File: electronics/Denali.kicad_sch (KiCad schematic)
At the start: 1 part, among them U1 kb2040

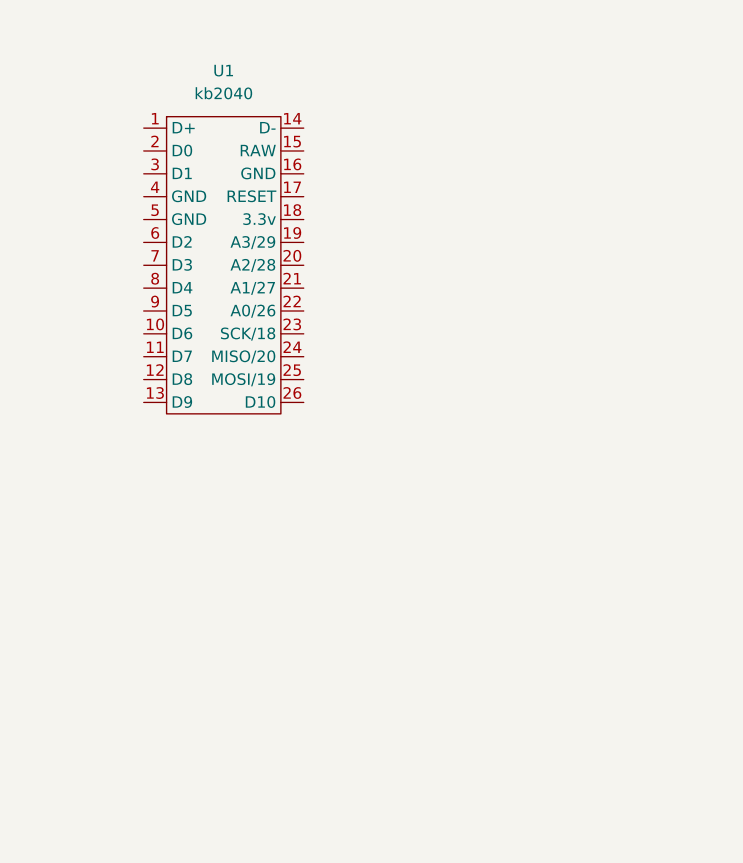
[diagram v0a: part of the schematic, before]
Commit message: add i2c headers to schematic
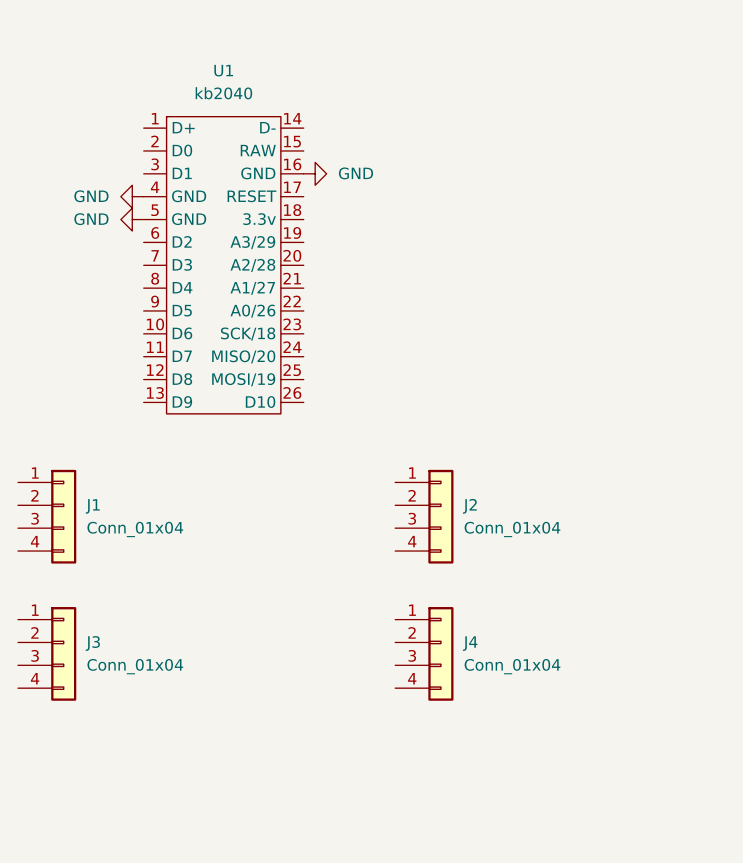
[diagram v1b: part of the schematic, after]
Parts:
- added J1, J2, J3, J4: Conn_01x04, symbol Connector_Generic:Conn_01x04
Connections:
- net GND: now reaches U1.16 (GND)
- net GND: now also U1.4 (GND), U1.5 (GND)
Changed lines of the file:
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@@
     (company "OSHMount Tech")
+  )
+  (symbol (lib_id "Connector_Generic:Conn_01x04") (at 36.83 92.71 0) (unit 1)
+    (in_bom yes) (on_board yes) (fields_autoplaced)
+    (property "Reference" "J3" (id 0) (at 39.37 92.7099 0)
+      (effects (font (size 1.27 1.27)) (justify left))
+    )
+    (property "Value" "Conn_01x04" (id 1) (at 39.37 95.2499 0)
+      (effects (font (size 1.27 1.27)) (justify left))
+    )
+    (property "Footprint" "" (id 2) (at 36.83 92.71 0)
+      (effects (font (size 1.27 1.27)) hide)
+    )
+    (property "Datasheet" "~" (id 3) (at 36.83 92.71 0)
+      (effects (font (size 1.27 1.27)) hide)
+    )
+    (pin "1")
+    (pin "2")
+    (pin "3")
+    (pin "4")
+  )
+  (symbol (lib_id "power:GND") (at 63.5 40.64 90) (unit 1)
+    (in_bom yes) (on_board yes) (fields_autoplaced)
+    (property "Reference" "#PWR01" (id 0) (at 69.85 40.64 0)
+      (effects (font (size 1.27 1.27)) hide)
+    )
+    (property "Value" "GND" (id 1) (at 67.31 40.6399 90)
+      (effects (font (size 1.27 1.27)) (justify right))
+    )
+    (property "Footprint" "" (id 2) (at 63.5 40.64 0)
+      (effects (font (size 1.27 1.27)) hide)
+    )
+    (property "Datasheet" "" (id 3) (at 63.5 40.64 0)
+      (effects (font (size 1.27 1.27)) hide)
+    )
+    (pin "1")
+  )
+  (symbol (lib_id "power:GND") (at 45.72 43.18 270) (unit 1)
+    (in_bom yes) (on_board yes) (fields_autoplaced)
+    (property "Reference" "#PWR02" (id 0) (at 39.37 43.18 0)
+      (effects (font (size 1.27 1.27)) hide)
+    )
+    (property "Value" "GND" (id 1) (at 41.91 43.1799 90)
+      (effects (font (size 1.27 1.27)) (justify right))
+    )
+    (property "Footprint" "" (id 2) (at 45.72 43.18 0)
+      (effects (font (size 1.27 1.27)) hide)
+    )
+    (property "Datasheet" "" (id 3) (at 45.72 43.18 0)
+      (effects (font (size 1.27 1.27)) hide)
+    )
+    (pin "1")
+  )
+  (symbol (lib_id "Connector_Generic:Conn_01x04") (at 78.74 77.47 0) (unit 1)
+    (in_bom yes) (on_board yes) (fields_autoplaced)
+    (property "Reference" "J2" (id 0) (at 81.28 77.4699 0)
+      (effects (font (size 1.27 1.27)) (justify left))
+    )
+    (property "Value" "Conn_01x04" (id 1) (at 81.28 80.0099 0)
+      (effects (font (size 1.27 1.27)) (justify left))
+    )
+    (property "Footprint" "" (id 2) (at 78.74 77.47 0)
+      (effects (font (size 1.27 1.27)) hide)
+    )
+    (property "Datasheet" "~" (id 3) (at 78.74 77.47 0)
+      (effects (font (size 1.27 1.27)) hide)
+    )
+    (pin "1")
+    (pin "2")
+    (pin "3")
+    (pin "4")
+  )
+  (symbol (lib_id "power:GND") (at 45.72 45.72 270) (unit 1)
+    (in_bom yes) (on_board yes) (fields_autoplaced)
+    (property "Reference" "#PWR03" (id 0) (at 39.37 45.72 0)
+      (effects (font (size 1.27 1.27)) hide)
+    )
+    (property "Value" "GND" (id 1) (at 41.91 45.7199 90)
+      (effects (font (size 1.27 1.27)) (justify right))
+    )
+    (property "Footprint" "" (id 2) (at 45.72 45.72 0)
+      (effects (font (size 1.27 1.27)) hide)
+    )
+    (property "Datasheet" "" (id 3) (at 45.72 45.72 0)
+      (effects (font (size 1.27 1.27)) hide)
+    )
+    (pin "1")
+  )
+  (symbol (lib_id "Connector_Generic:Conn_01x04") (at 36.83 77.47 0) (unit 1)
+    (in_bom yes) (on_board yes) (fields_autoplaced)
+    (property "Reference" "J1" (id 0) (at 39.37 77.4699 0)
+      (effects (font (size 1.27 1.27)) (justify left))
+    )
+    (property "Value" "Conn_01x04" (id 1) (at 39.37 80.0099 0)
+      (effects (font (size 1.27 1.27)) (justify left))
+    )
+    (property "Footprint" "" (id 2) (at 36.83 77.47 0)
+      (effects (font (size 1.27 1.27)) hide)
+    )
+    (property "Datasheet" "~" (id 3) (at 36.83 77.47 0)
+      (effects (font (size 1.27 1.27)) hide)
+    )
+    (pin "1")
+    (pin "2")
+    (pin "3")
+    (pin "4")
   )
   (symbol (lib_id "kb2040:kb2040") (at 48.26 30.48 0) (unit 1)
@@
     (pin "9")
   )
+  (symbol (lib_id "Connector_Generic:Conn_01x04") (at 78.74 92.71 0) (unit 1)
+    (in_bom yes) (on_board yes) (fields_autoplaced)
+    (property "Reference" "J4" (id 0) (at 81.28 92.7099 0)
+      (effects (font (size 1.27 1.27)) (justify left))
+    )
+    (property "Value" "Conn_01x04" (id 1) (at 81.28 95.2499 0)
+      (effects (font (size 1.27 1.27)) (justify left))
+    )
+    (property "Footprint" "" (id 2) (at 78.74 92.71 0)
+      (effects (font (size 1.27 1.27)) hide)
+    )
+    (property "Datasheet" "~" (id 3) (at 78.74 92.71 0)
+      (effects (font (size 1.27 1.27)) hide)
+    )
+    (pin "1")
+    (pin "2")
+    (pin "3")
+    (pin "4")
+  )
   (sheet (at 223.52 57.15) (size 55.88 29.21) (fields_autoplaced)
     (stroke (width 0.1524) (type solid) (color 0 0 0 0))
@@
   )
   (symbol_instances
+    (path "/3c636b90-6cff-4fb4-a25c-6bcc35fc5db5"
+      (reference "#PWR01") (unit 1) (value "GND") (footprint "")
+    )
+    (path "/5494e583-f9db-456a-afdd-de147d0830de"
+      (reference "#PWR02") (unit 1) (value "GND") (footprint "")
+    )
+    (path "/cb4c4818-e2e2-496c-a0a5-21b8e31346a2"
+      (reference "#PWR03") (unit 1) (value "GND") (footprint "")
+    )
+    (path "/cb8c502c-8777-4908-bcec-a417c39cf62d/d9917178-7fb0-4e2e-842f-4275ce422ab9"
+      (reference "#PWR04") (unit 1) (value "GND") (footprint "")
+    )
+    (path "/ebc26802-b705-4f7c-957e-e7926732b9b9"
+      (reference "J1") (unit 1) (value "Conn_01x04") (footprint "")
+    )
+    (path "/a45f7474-1dac-4555-b4eb-1558d6f8cac5"
+      (reference "J2") (unit 1) (value "Conn_01x04") (footprint "")
+    )
+    (path "/20e8a1b1-fb6d-4633-8b2b-8f799e8b5ea2"
+      (reference "J3") (unit 1) (value "Conn_01x04") (footprint "")
+    )
+    (path "/fd702f30-033f-429e-be5a-c6df39b69222"
+      (reference "J4") (unit 1) (value "Conn_01x04") (footprint "")
+    )
+    (path "/cb8c502c-8777-4908-bcec-a417c39cf62d/6bf10c56-aa23-4912-9293-34fc92378a56"
+      (reference "J5") (unit 1) (value "Conn_01x04") (footprint "")
+    )
+    (path "/cb8c502c-8777-4908-bcec-a417c39cf62d/467df09e-9638-4550-9bd2-b6838720626d"
+      (reference "J6") (unit 1) (value "Conn_01x04") (footprint "")
+    )
+    (path "/cb8c502c-8777-4908-bcec-a417c39cf62d/97290991-4bad-4058-babf-e02b47c79857"
+      (reference "J7") (unit 1) (value "Conn_01x04") (footprint "")
+    )
+    (path "/cb8c502c-8777-4908-bcec-a417c39cf62d/47166bff-52bf-422b-8850-2334c5fc2b64"
+      (reference "J8") (unit 1) (value "Conn_01x04") (footprint "")
+    )
+    (path "/155910c1-5cb8-473e-a85a-4a0b3c288dbb/26c44fa1-a33a-4233-b61f-9ba0a6e97f21"
+      (reference "J9") (unit 1) (value "Conn_01x04") (footprint "")
+    )
+    (path "/155910c1-5cb8-473e-a85a-4a0b3c288dbb/4cbbed99-cd17-4414-aa03-ae8cf56abd25"
+      (reference "J10") (unit 1) (value "Conn_01x04") (footprint "")
+    )
+    (path "/155910c1-5cb8-473e-a85a-4a0b3c288dbb/19cf36b9-8f8a-4263-a851-503d275c3110"
+      (reference "J11") (unit 1) (value "Conn_01x04") (footprint "")
+    )
+    (path "/155910c1-5cb8-473e-a85a-4a0b3c288dbb/391adc4e-7a90-4d18-a1a0-2e3697b19a59"
+      (reference "J12") (unit 1) (value "Conn_01x04") (footprint "")
+    )
+    (path "/735c9d38-f728-480f-bd34-fe3dcf6ce5fc/5267bdd7-3ca6-4d8f-9cbd-07da5ae7bded"
+      (reference "J13") (unit 1) (value "Conn_01x04") (footprint "")
+    )
+    (path "/735c9d38-f728-480f-bd34-fe3dcf6ce5fc/c399b4da-ccd3-4abc-9d74-21b4c650db57"
+      (reference "J14") (unit 1) (value "Conn_01x04") (footprint "")
+    )
+    (path "/735c9d38-f728-480f-bd34-fe3dcf6ce5fc/c60faae4-0ec1-4a63-89c9-10bd0efb94ad"
+      (reference "J15") (unit 1) (value "Conn_01x04") (footprint "")
+    )
+    (path "/735c9d38-f728-480f-bd34-fe3dcf6ce5fc/17c22edb-a9bf-4669-8ce1-6d6524df7103"
+      (reference "J16") (unit 1) (value "Conn_01x04") (footprint "")
+    )
+    (path "/4bf7e2ed-3223-497b-8c9a-4917a7c5fbb6/e6031ff9-7e93-4b94-81c2-39671e480ce9"
+      (reference "J17") (unit 1) (value "Conn_01x04") (footprint "")
+    )
+    (path "/4bf7e2ed-3223-497b-8c9a-4917a7c5fbb6/ddbe0da8-11aa-43c6-bcd0-93e5afd7807e"
+      (reference "J18") (unit 1) (value "Conn_01x04") (footprint "")
+    )
+    (path "/4bf7e2ed-3223-497b-8c9a-4917a7c5fbb6/483376b0-73d7-40cc-a38f-260f50350d58"
+      (reference "J19") (unit 1) (value "Conn_01x04") (footprint "")
+    )
+    (path "/4bf7e2ed-3223-497b-8c9a-4917a7c5fbb6/d43e46b5-e1e1-4f64-a7a8-3db67aff9317"
+      (reference "J20") (unit 1) (value "Conn_01x04") (footprint "")
+    )
     (path "/cb8c502c-8777-4908-bcec-a417c39cf62d/dff9b877-632a-4706-bfaf-075eb50bfdd1"
       (reference "SW1") (unit 1) (value "SW_SPST") (footprint "Kailh:Kailh_socket_MX")

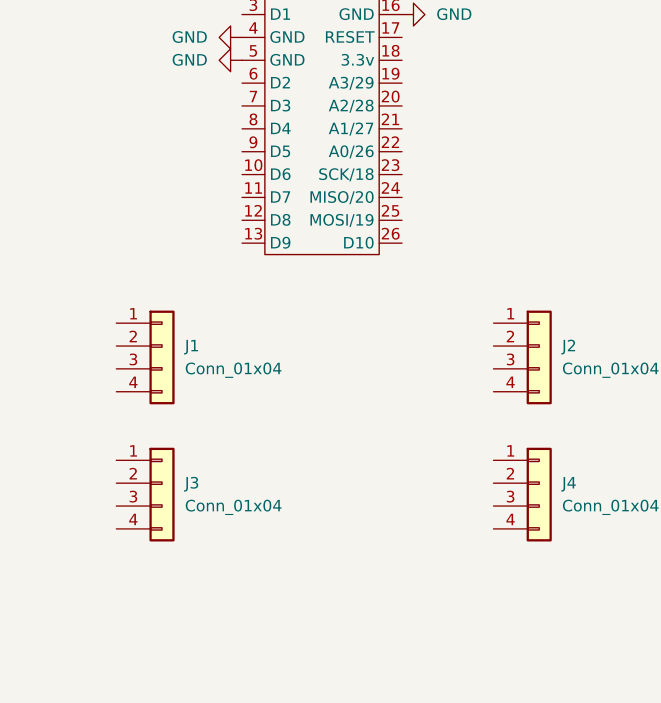
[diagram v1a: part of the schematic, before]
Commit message: label switch nets
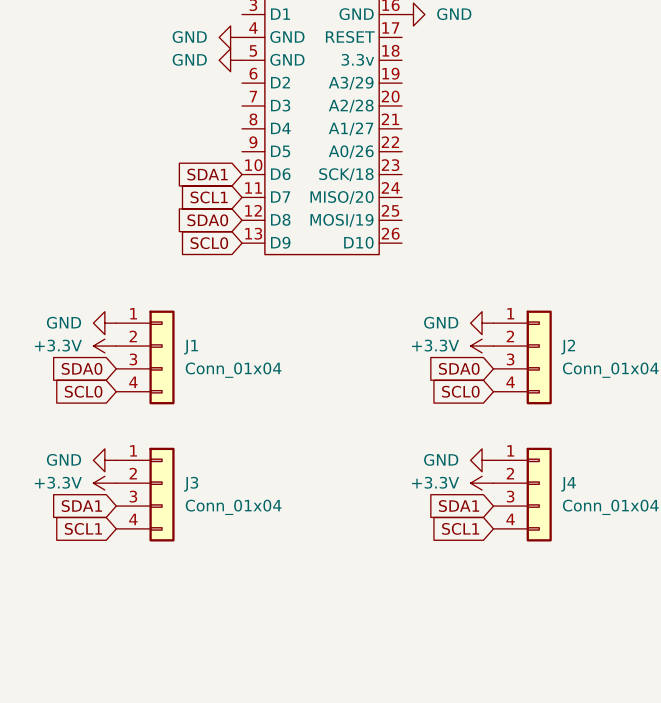
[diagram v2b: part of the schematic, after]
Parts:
- U1: footprint KeeBoar:kb2040 -> kb2040:kb2040
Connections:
- net GND: now also J1.1 (Pin_1), J2.1 (Pin_1), J3.1 (Pin_1), J4.1 (Pin_1)
- net +3V3: now reaches J3.2 (Pin_2)
- net +3V3: now also J1.2 (Pin_2), J2.2 (Pin_2), J4.2 (Pin_2)
- net SDA1: now reaches J3.3 (Pin_3)
- net SDA1: now also J4.3 (Pin_3), U1.10 (D6)
- net SCL1: now reaches J3.4 (Pin_4)
- net SCL1: now also J4.4 (Pin_4), U1.11 (D7)
- net SDA0: now reaches J2.3 (Pin_3)
- net SDA0: now also J1.3 (Pin_3), U1.12 (D8)
- net SCL0: now reaches J2.4 (Pin_4)
- net SCL0: now also J1.4 (Pin_4), U1.13 (D9)

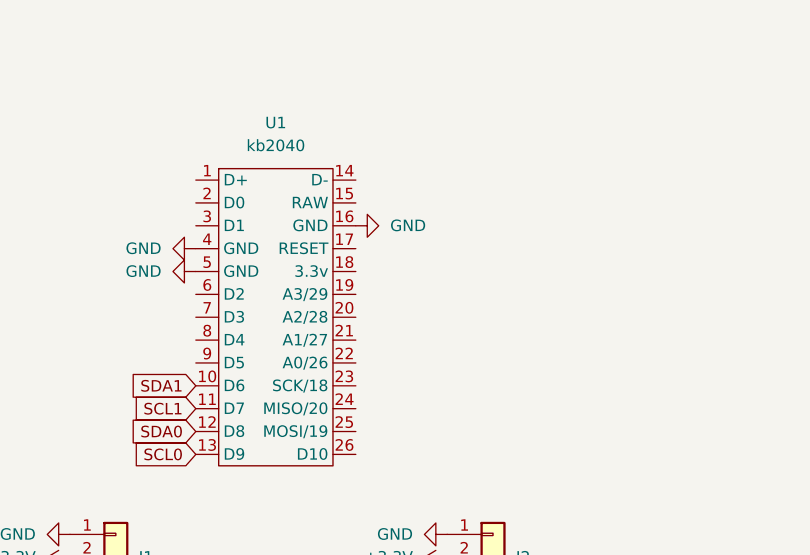
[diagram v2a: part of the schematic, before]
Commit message: move some switches
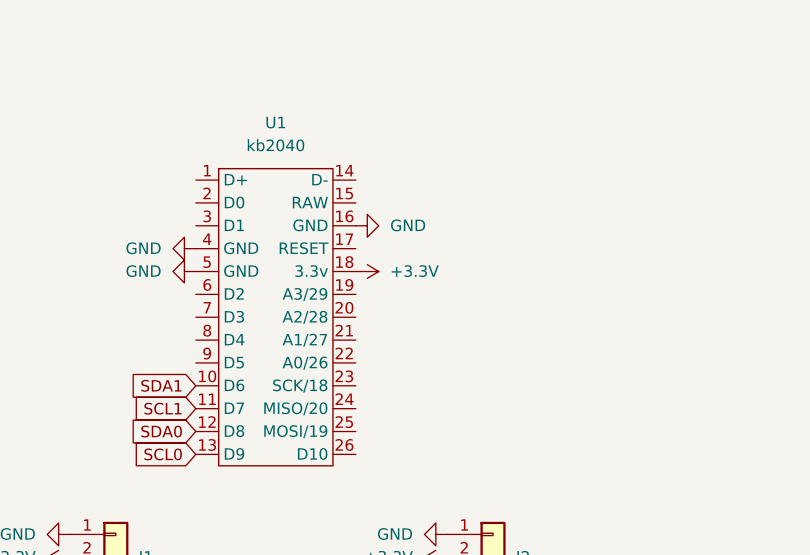
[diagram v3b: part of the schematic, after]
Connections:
- net +3V3: now also U1.18 (3.3v)
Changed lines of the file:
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@@
     (pin "4")
+  )
+  (symbol (lib_id "power:+3.3V") (at 63.5 45.72 270) (unit 1)
+    (in_bom yes) (on_board yes) (fields_autoplaced)
+    (property "Reference" "#PWR?" (id 0) (at 59.69 45.72 0)
+      (effects (font (size 1.27 1.27)) hide)
+    )
+    (property "Value" "+3.3V" (id 1) (at 67.31 45.7199 90)
+      (effects (font (size 1.27 1.27)) (justify left))
+    )
+    (property "Footprint" "" (id 2) (at 63.5 45.72 0)
+      (effects (font (size 1.27 1.27)) hide)
+    )
+    (property "Datasheet" "" (id 3) (at 63.5 45.72 0)
+      (effects (font (size 1.27 1.27)) hide)
+    )
+    (pin "1")
   )
   (symbol (lib_id "kb2040:kb2040") (at 48.26 30.48 0) (unit 1)
@@
       (reference "#PWR047") (unit 1) (value "GND") (footprint "")
     )
+    (path "/f621dca6-2e8a-4ab7-8a4b-480d0a1e895d"
+      (reference "#PWR?") (unit 1) (value "+3.3V") (footprint "")
+    )
     (path "/ebc26802-b705-4f7c-957e-e7926732b9b9"
